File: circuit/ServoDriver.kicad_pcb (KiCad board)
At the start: 2 copper layers, 47 parts, among them IC1 TLP521, IC2 TLP521, IC3 TLP521, IC4 TLP521, IC5 TLP521, IC6 TLP521, J1 RJ45_8pin, J2 RJ45_8pin, J3 servo0, J4 servo1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

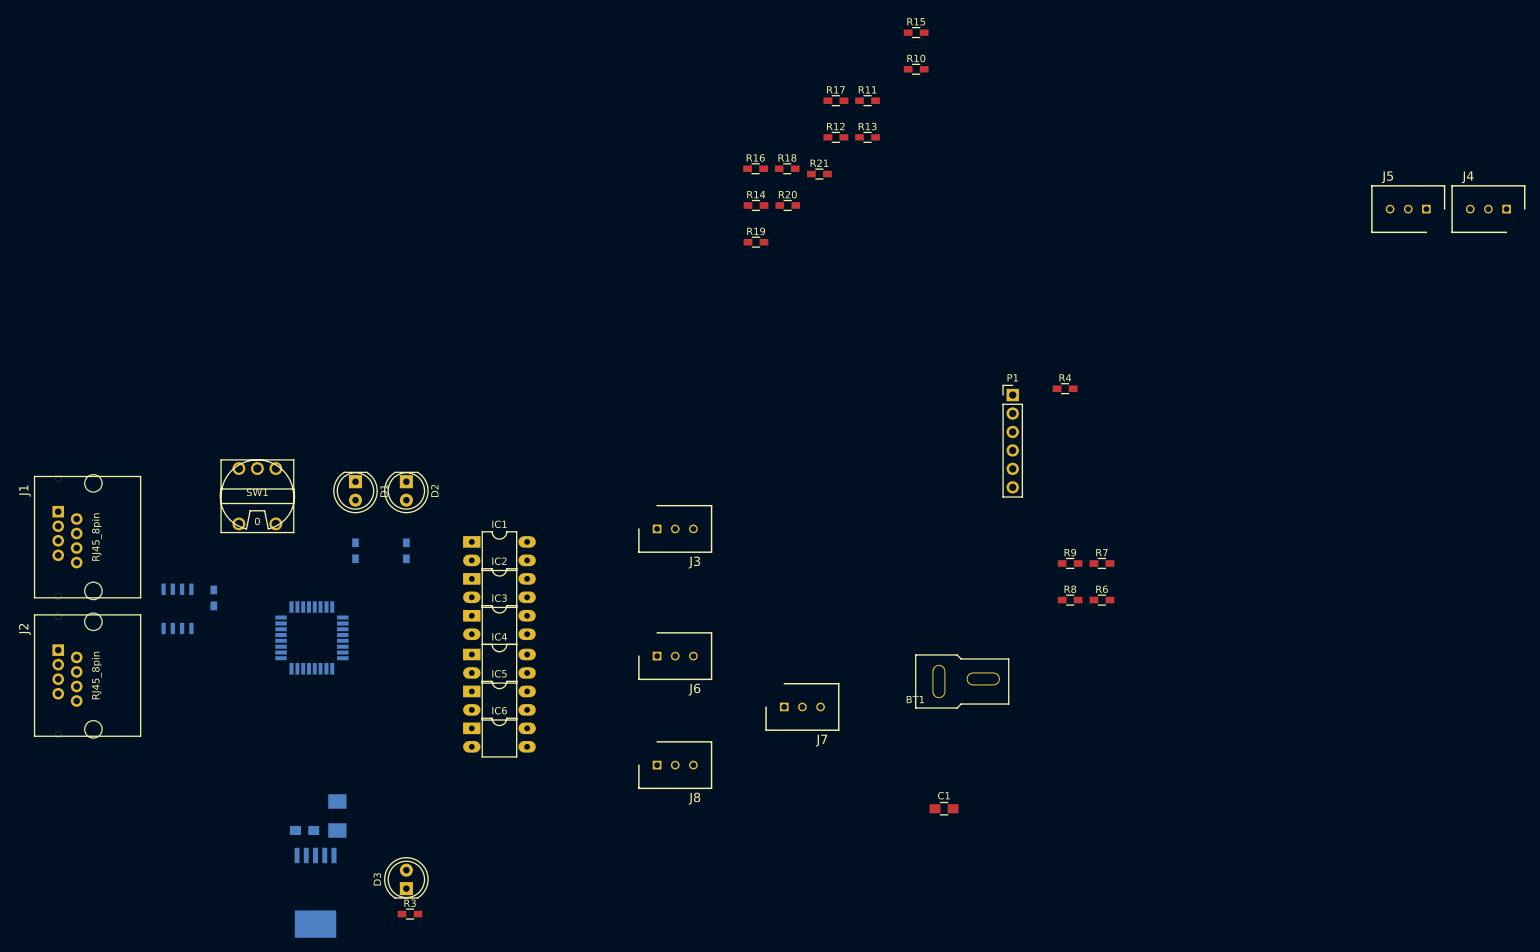
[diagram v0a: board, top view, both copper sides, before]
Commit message: 実態配線図の部品配置を大まかに決定
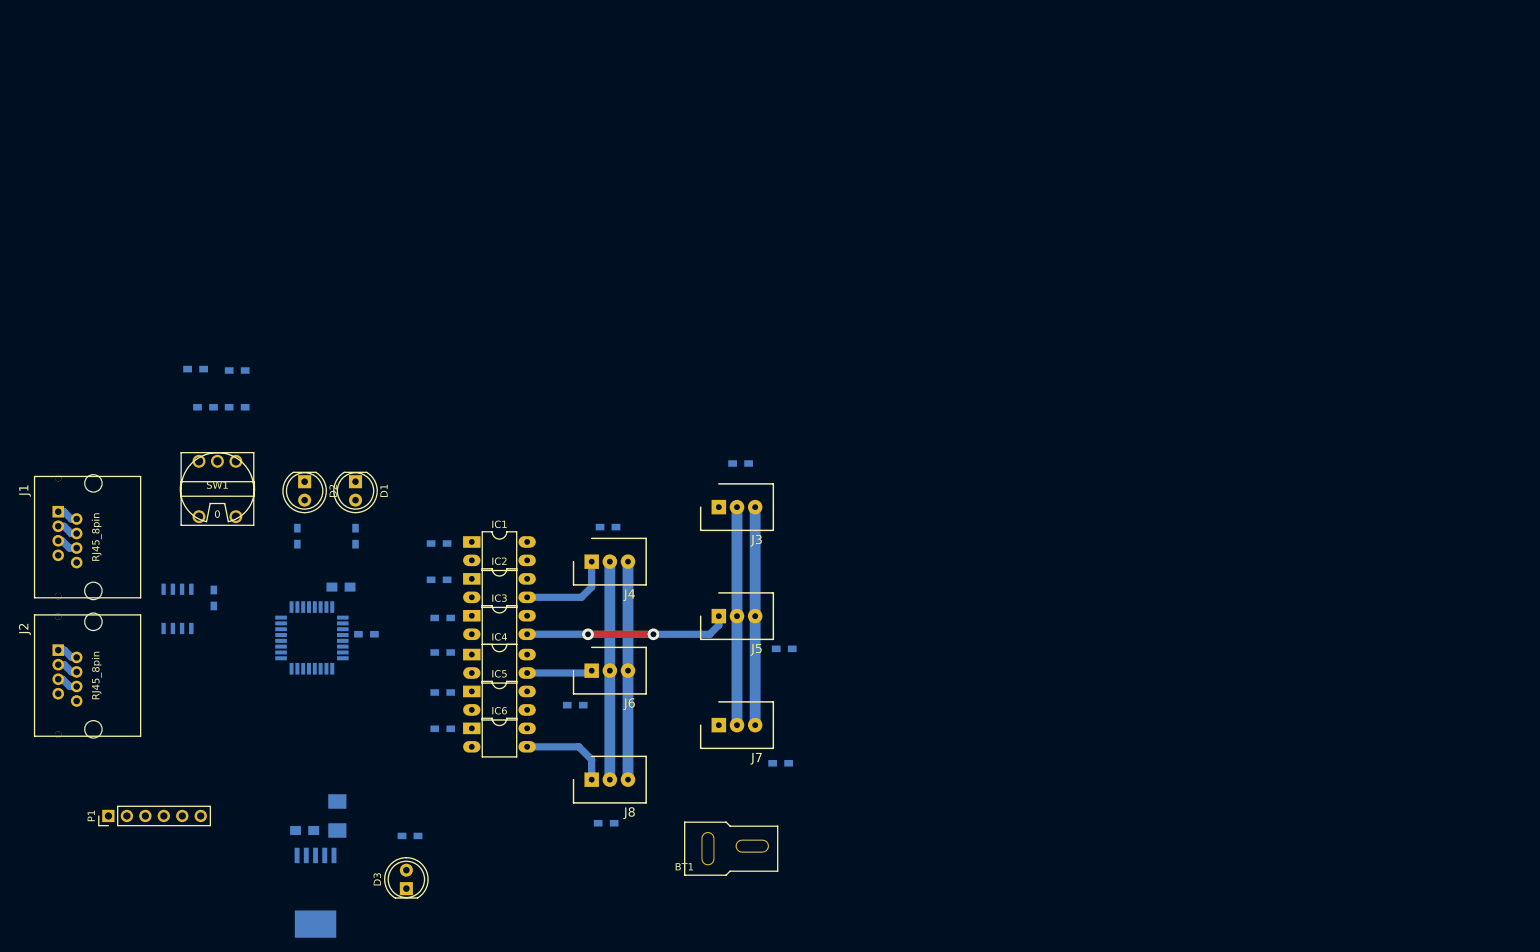
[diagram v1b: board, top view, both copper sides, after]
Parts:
- C1, R10, R11, R12, R13, R14, R15, R16, R17, R18, R19, R20, R21, R3, R4, R6, R7, R8, R9: moved to B.Cu
- J3, J4, J5, J6, J7, J8: footprint YASU:XA_3Pin -> YASU:XA_3Pin_LP
- moved P1 137.3 mm to (92.0, 126.0), turned to 90 degrees
- moved J4 134.9 mm to (158.5, 91.0), turned to 180 degrees
- moved R8 124.5 mm to (104.0, 64.5)
- moved R6 123.1 mm to (109.7, 64.7)
- moved R7 120.9 mm to (109.7, 69.8)
- moved R9 120.9 mm to (105.4, 69.8)
- moved J5 112.3 mm to (176.0, 98.5), turned to 180 degrees
- moved R4 101.9 mm to (127.5, 101.0), turned to 180 degrees
- moved R17 97.8 mm to (138.0, 109.0), turned to 180 degrees
- moved R21 94.0 mm to (160.5, 127.0)
- moved R10 92.6 mm to (137.5, 88.5), turned to 180 degrees
- moved R18 90.5 mm to (138.0, 114.0), turned to 180 degrees
- moved R11 88.5 mm to (137.5, 93.5), turned to 180 degrees
- moved C1 88.4 mm to (124.0, 94.5), turned to 180 degrees
- moved R15 86.7 mm to (185.0, 103.0)
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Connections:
- IC1 pad 1: /Servo0 -> Net-(IC1-Pad1)
- IC1 pad 2: Net-(IC1-Pad2) -> GND
- IC2 pad 1: /Servo1 -> Net-(IC2-Pad1)
- IC2 pad 2: Net-(IC2-Pad2) -> GND
- IC3 pad 1: /Servo2 -> Net-(IC3-Pad1)
- IC3 pad 2: Net-(IC3-Pad2) -> GND
- IC4 pad 1: /Servo3 -> Net-(IC4-Pad1)
- IC4 pad 2: Net-(IC4-Pad2) -> GND
- IC5 pad 1: /Servo4 -> Net-(IC5-Pad1)
- IC5 pad 2: Net-(IC5-Pad2) -> GND
- IC6 pad 1: /Servo5 -> Net-(IC6-Pad1)
- IC6 pad 2: Net-(IC6-Pad2) -> GND
- R10 pad 1: Net-(IC1-Pad2) -> Net-(IC1-Pad1)
- R10 pad 2: GND -> /Servo0
- R11 pad 1: Net-(IC2-Pad2) -> Net-(IC2-Pad1)
- R11 pad 2: GND -> /Servo1
- R12 pad 1: Net-(IC3-Pad2) -> Net-(IC3-Pad1)
- R12 pad 2: GND -> /Servo2
- R16 pad 1: Net-(IC4-Pad2) -> Net-(IC4-Pad1)
- R16 pad 2: GND -> /Servo3
- R17 pad 1: Net-(IC5-Pad2) -> Net-(IC5-Pad1)
- R17 pad 2: GND -> /Servo4
- R18 pad 1: Net-(IC6-Pad2) -> Net-(IC6-Pad1)
- R18 pad 2: GND -> /Servo5
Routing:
- net GNDPWR: track 0.00 -> 60.0 mm
- net +7.4V: track 0.00 -> 60.0 mm
- net Net-(IC3-Pad3): track 0.00 -> 28.1 mm, vias 0 -> 2
- net Net-(IC2-Pad3): track 0.00 -> 13.0 mm
- net Net-(IC6-Pad3): track 0.00 -> 12.4 mm
- net Net-(IC4-Pad3): track 0.00 -> 9.01 mm
- net GND: track 0.00 -> 6.20 mm
- net +5V: track 0.00 -> 5.91 mm
- net +12V: track 0.00 -> 5.91 mm

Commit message: モータ側の配線完了
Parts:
- R13, R14, R15, R19, R20, R21: footprint Resistors_SMD:R_0603_HandSoldering -> Resistors_THT:R_Axial_DIN0207_L6.3mm_D2.5mm_P7.62mm_Horizontal; moved to F.Cu
- moved R13 12.3 mm to (173.5, 88.5)
- moved R15 11.5 mm to (173.5, 103.5)
- moved R20 11.0 mm to (173.5, 118.5)
- moved R14 11.0 mm to (155.8, 96.0)
- moved R21 4.61 mm to (156.0, 126.0)
- moved BT1 4.01 mm to (170.5, 130.2)
- moved R19 0.56 mm to (155.8, 111.0)
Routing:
- net +7.4V: track 60.0 -> 176.3 mm
- net GNDPWR: track 60.0 -> 107.4 mm
- net Net-(IC1-Pad3): track 0.00 -> 34.3 mm, vias 0 -> 2
- net Net-(IC5-Pad3): track 0.00 -> 32.9 mm, vias 0 -> 2
- net Net-(IC4-Pad3): track 9.01 -> 15.9 mm
- net Net-(IC6-Pad3): track 12.4 -> 19.1 mm
- net Net-(IC3-Pad3): track 28.1 -> 31.2 mm

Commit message: コアを斜めにした
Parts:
- moved C2 12.9 mm to (125.8, 117.0)
- moved C3 12.9 mm to (130.2, 115.0)
- moved U3 12.9 mm to (127.2, 121.0)
- moved D3 10.3 mm to (139.8, 128.2)
- moved R3 10.3 mm to (140.2, 121.0)
- moved U1 6.82 mm to (126.8, 102.5), turned to 225 degrees
- moved C1 6.36 mm to (119.5, 90.0)
- moved R4 5.15 mm to (130.0, 96.5), turned to 315 degrees

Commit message: 基板外形線の追加
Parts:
- moved C1 8.06 mm to (126.5, 94.0)
- moved J1 5.50 mm to (87.6, 93.1)
- moved U2 5.00 mm to (101.5, 102.5)
- moved J2 4.50 mm to (87.6, 111.2)
- moved R10 0.79 mm to (138.2, 88.2)
- moved R11 0.75 mm to (138.2, 93.5)
- moved R12 0.35 mm to (138.2, 98.5)
- moved R16 0.35 mm to (138.2, 103.8)
- moved R18 0.25 mm to (138.2, 114.0)
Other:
- board outline added: 102.5 x 54.5 mm
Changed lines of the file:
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@@
     (area 78.9718 61.975 195.176192 142.956775)
     (thickness 1.6)
-    (drawings 0)
-    (tracks 137)
+    (drawings 4)
+    (tracks 136)
     (zones 0)
     (modules 47)
@@
     (pad_to_mask_clearance 0.2)
     (aux_axis_origin 0 0)
-    (visible_elements 7FFFFFFF)
+    (visible_elements 7FFFF7FF)
     (pcbplotparams
       (layerselection 0x00030_80000001)
@@
     (add_net "Net-(U3-Pad4)")
   )
+  (module Resistors_SMD:R_0603_HandSoldering (layer B.Cu)
+    (at 138.25 88.25 180)
+    (descr "Resistor SMD 0603, hand soldering")
+    (tags "resistor 0603")
+    (attr smd)
+    (fp_text reference R10 (at 0 1.45 180) (layer B.SilkS)
+      (effects (font (size 1 1) (thickness 0.15)) (justify mirror))
+    )
+    (fp_text value 1k (at 0 -1.55 180) (layer B.Fab)
+      (effects (font (size 1 1) (thickness 0.15)) (justify mirror))
+    )
+    (fp_text user %R (at 0 0 180) (layer B.Fab)
+      (effects (font (size 0.4 0.4) (thickness 0.075)) (justify mirror))
+    )
+    (fp_line (start -0.8 -0.4) (end -0.8 0.4) (layer B.Fab) (width 0.1))
+    (fp_line (start 0.8 -0.4) (end -0.8 -0.4) (layer B.Fab) (width 0.1))
+    (fp_line (start 0.8 0.4) (end 0.8 -0.4) (layer B.Fab) (width 0.1))
+    (fp_line (start -0.8 0.4) (end 0.8 0.4) (layer B.Fab) (width 0.1))
+    (fp_line (start 0.5 -0.68) (end -0.5 -0.68) (layer B.SilkS) (width 0.12))
+    (fp_line (start -0.5 0.68) (end 0.5 0.68) (layer B.SilkS) (width 0.12))
+    (fp_line (start -1.96 0.7) (end 1.95 0.7) (layer B.CrtYd) (width 0.05))
+    (fp_line (start -1.96 0.7) (end -1.96 -0.7) (layer B.CrtYd) (width 0.05))
+    (fp_line (start 1.95 -0.7) (end 1.95 0.7) (layer B.CrtYd) (width 0.05))
+    (fp_line (start 1.95 -0.7) (end -1.96 -0.7) (layer B.CrtYd) (width 0.05))
+    (pad 1 smd rect (at -1.1 0 180) (size 1.2 0.9) (layers B.Cu B.Paste B.Mask)
+      (net 49 "Net-(IC1-Pad1)"))
+    (pad 2 smd rect (at 1.1 0 180) (size 1.2 0.9) (layers B.Cu B.Paste B.Mask)
+      (net 9 /Servo0))
+    (model ${KISYS3DMOD}/Resistors_SMD.3dshapes/R_0603.wrl
+      (at (xyz 0 0 0))
+      (scale (xyz 1 1 1))
+      (rotate (xyz 0 0 0))
+    )
+  )
   (module YASU:XA_3Pin_LP (layer F.Cu)
     (at 176 98.5 180)
@@
   )
   (module Capacitors_SMD:C_0805_HandSoldering (layer B.Cu)
-    (at 119.5 90 180)
+    (at 126.5 94 180)
     (descr "Capacitor SMD 0805, hand soldering")
     (tags "capacitor 0805")
@@
   )
   (module robocon_pcb:7810-8P8C (layer F.Cu)
-    (at 87.63 87.63 90)
+    (at 87.63 93.13 90)
     (tags RJ45)
     (fp_text reference J1 (at 6.477 -7.239 90) (layer F.SilkS)
@@
   )
   (module robocon_pcb:7810-8P8C (layer F.Cu)
-    (at 87.63 106.68 90)
+    (at 87.63 111.18 90)
     (tags RJ45)
     (fp_text reference J2 (at 6.477 -7.239 90) (layer F.SilkS)
@@
   )
   (module Resistors_SMD:R_0603_HandSoldering (layer B.Cu)
-    (at 137.5 88.5 180)
-    (descr "Resistor SMD 0603, hand soldering")
-    (tags "resistor 0603")
-    (attr smd)
-    (fp_text reference R10 (at 0 1.45 180) (layer B.SilkS)
-      (effects (font (size 1 1) (thickness 0.15)) (justify mirror))
-    )
-    (fp_text value 1k (at 0 -1.55 180) (layer B.Fab)
-      (effects (font (size 1 1) (thickness 0.15)) (justify mirror))
-    )
-    (fp_text user %R (at 0 0 180) (layer B.Fab)
-      (effects (font (size 0.4 0.4) (thickness 0.075)) (justify mirror))
-    )
-    (fp_line (start -0.8 -0.4) (end -0.8 0.4) (layer B.Fab) (width 0.1))
-    (fp_line (start 0.8 -0.4) (end -0.8 -0.4) (layer B.Fab) (width 0.1))
-    (fp_line (start 0.8 0.4) (end 0.8 -0.4) (layer B.Fab) (width 0.1))
-    (fp_line (start -0.8 0.4) (end 0.8 0.4) (layer B.Fab) (width 0.1))
-    (fp_line (start 0.5 -0.68) (end -0.5 -0.68) (layer B.SilkS) (width 0.12))
-    (fp_line (start -0.5 0.68) (end 0.5 0.68) (layer B.SilkS) (width 0.12))
-    (fp_line (start -1.96 0.7) (end 1.95 0.7) (layer B.CrtYd) (width 0.05))
-    (fp_line (start -1.96 0.7) (end -1.96 -0.7) (layer B.CrtYd) (width 0.05))
-    (fp_line (start 1.95 -0.7) (end 1.95 0.7) (layer B.CrtYd) (width 0.05))
-    (fp_line (start 1.95 -0.7) (end -1.96 -0.7) (layer B.CrtYd) (width 0.05))
-    (pad 1 smd rect (at -1.1 0 180) (size 1.2 0.9) (layers B.Cu B.Paste B.Mask)
-      (net 49 "Net-(IC1-Pad1)"))
-    (pad 2 smd rect (at 1.1 0 180) (size 1.2 0.9) (layers B.Cu B.Paste B.Mask)
-      (net 9 /Servo0))
-    (model ${KISYS3DMOD}/Resistors_SMD.3dshapes/R_0603.wrl
-      (at (xyz 0 0 0))
-      (scale (xyz 1 1 1))
-      (rotate (xyz 0 0 0))
-    )
-  )
-  (module Resistors_SMD:R_0603_HandSoldering (layer B.Cu)
-    (at 137.5 93.5 180)
+    (at 138.25 93.5 180)
     (descr "Resistor SMD 0603, hand soldering")
     (tags "resistor 0603")
@@
   )
   (module Resistors_SMD:R_0603_HandSoldering (layer B.Cu)
-    (at 138 98.75 180)
+    (at 138.25 98.5 180)
     (descr "Resistor SMD 0603, hand soldering")
     (tags "resistor 0603")
@@
   )
   (module Resistors_SMD:R_0603_HandSoldering (layer B.Cu)
-    (at 138 103.5 180)
+    (at 138.25 103.75 180)
     (descr "Resistor SMD 0603, hand soldering")
     (tags "resistor 0603")
@@
   )
   (module Resistors_SMD:R_0603_HandSoldering (layer B.Cu)
-    (at 138 114 180)
+    (at 138.25 114 180)
     (descr "Resistor SMD 0603, hand soldering")
     (tags "resistor 0603")
@@
   )
   (module Housings_SOIC:SOIC-8_3.9x4.9mm_Pitch1.27mm (layer B.Cu)
-    (at 101.5 97.5 90)
+    (at 101.5 102.5 90)
     (descr "8-Lead Plastic Small Outline (SN) - Narrow, 3.90 mm Body [SOIC] (see Microchip Packaging Specification 00000049BS.pdf)")
     (tags "SOIC 1.27")
@@
     )
   )
+  (gr_line (start 81.5 134.25) (end 184 134.25) (angle 90) (layer Edge.Cuts) (width 0.15))
+  (gr_line (start 81.5 79.75) (end 81.5 134.25) (angle 90) (layer Edge.Cuts) (width 0.15))
+  (gr_line (start 184 79.75) (end 81.5 79.75) (angle 90) (layer Edge.Cuts) (width 0.15))
+  (gr_line (start 184 134.25) (end 184 79.75) (angle 90) (layer Edge.Cuts) (width 0.15))
   (segment (start 161 88.75) (end 161 83.5) (width 1.5) (layer B.Cu) (net 1))
   (segment (start 163.75 80.75) (end 175.75 80.75) (width 1.5) (layer B.Cu) (net 1))
@@
   (segment (start 163.5 106) (end 163.5 97.75) (width 1.5) (layer B.Cu) (net 2))
   (segment (start 163.5 97.75) (end 163.5 91) (width 1.5) (layer B.Cu) (net 2))
-  (segment (start 85.09 107.18) (end 85.68 107.18) (width 1) (layer B.Cu) (net 4))
-  (segment (start 85.68 107.18) (end 86.68 108.18) (width 1) (layer B.Cu) (net 4))
-  (segment (start 86.68 108.18) (end 87.63 108.18) (width 1) (layer B.Cu) (net 4))
-  (segment (start 85.09 88.13) (end 85.63 88.13) (width 1) (layer B.Cu) (net 4))
-  (segment (start 85.63 88.13) (end 86.63 89.13) (width 1) (layer B.Cu) (net 4))
-  (segment (start 86.63 89.13) (end 87.63 89.13) (width 1) (layer B.Cu) (net 4))
-  (segment (start 85.09 88.13) (end 85.38 88.13) (width 1) (layer B.Cu) (net 4))
-  (segment (start 85.09 105.18) (end 85.93 105.18) (width 1) (layer B.Cu) (net 5))
-  (segment (start 85.93 105.18) (end 86.93 106.18) (width 1) (layer B.Cu) (net 5))
-  (segment (start 86.93 106.18) (end 87.63 106.18) (width 1) (layer B.Cu) (net 5))
-  (segment (start 87.63 87.13) (end 86.88 87.13) (width 1) (layer B.Cu) (net 5))
-  (segment (start 86.88 87.13) (end 85.88 86.13) (width 1) (layer B.Cu) (net 5))
-  (segment (start 85.88 86.13) (end 85.09 86.13) (width 1) (layer B.Cu) (net 5))
-  (segment (start 136 88.5) (end 136.4 88.5) (width 0.5) (layer B.Cu) (net 9))
+  (segment (start 85.09 111.68) (end 85.68 111.68) (width 1) (layer B.Cu) (net 4))
+  (segment (start 85.68 111.68) (end 86.68 112.68) (width 1) (layer B.Cu) (net 4))
+  (segment (start 86.68 112.68) (end 87.63 112.68) (width 1) (layer B.Cu) (net 4))
+  (segment (start 85.09 93.63) (end 85.63 93.63) (width 1) (layer B.Cu) (net 4))
+  (segment (start 85.63 93.63) (end 86.63 94.63) (width 1) (layer B.Cu) (net 4))
+  (segment (start 86.63 94.63) (end 87.63 94.63) (width 1) (layer B.Cu) (net 4))
+  (segment (start 85.09 93.63) (end 85.38 93.63) (width 1) (layer B.Cu) (net 4))
+  (segment (start 85.09 109.68) (end 85.93 109.68) (width 1) (layer B.Cu) (net 5))
+  (segment (start 85.93 109.68) (end 86.93 110.68) (width 1) (layer B.Cu) (net 5))
+  (segment (start 86.93 110.68) (end 87.63 110.68) (width 1) (layer B.Cu) (net 5))
+  (segment (start 87.63 92.63) (end 86.88 92.63) (width 1) (layer B.Cu) (net 5))
+  (segment (start 86.88 92.63) (end 85.88 91.63) (width 1) (layer B.Cu) (net 5))
+  (segment (start 85.88 91.63) (end 85.09 91.63) (width 1) (layer B.Cu) (net 5))
   (segment (start 176 83.5) (end 176 84.25) (width 1) (layer B.Cu) (net 10))
   (segment (start 176 84.25) (end 174.5 85.75) (width 1) (layer B.Cu) (net 10))
@@
   (segment (start 158.5 118.25) (end 158.5 121) (width 1) (layer B.Cu) (net 20))
   (segment (start 156.734 116.484) (end 158.5 118.25) (width 1) (layer B.Cu) (net 20))
-  (segment (start 85.09 103.18) (end 85.93 103.18) (width 1) (layer B.Cu) (net 22))
-  (segment (start 85.93 103.18) (end 86.93 104.18) (width 1) (layer B.Cu) (net 22))
-  (segment (start 86.93 104.18) (end 87.63 104.18) (width 1) (layer B.Cu) (net 22))
-  (segment (start 85.09 84.13) (end 85.88 84.13) (width 1) (layer B.Cu) (net 22))
-  (segment (start 85.88 84.13) (end 86.88 85.13) (width 1) (layer B.Cu) (net 22))
-  (segment (start 86.88 85.13) (end 87.63 85.13) (width 1) (layer B.Cu) (net 22))
+  (segment (start 85.09 107.68) (end 85.93 107.68) (width 1) (layer B.Cu) (net 22))
+  (segment (start 85.93 107.68) (end 86.93 108.68) (width 1) (layer B.Cu) (net 22))
+  (segment (start 86.93 108.68) (end 87.63 108.68) (width 1) (layer B.Cu) (net 22))
+  (segment (start 85.09 89.63) (end 85.88 89.63) (width 1) (layer B.Cu) (net 22))
+  (segment (start 85.88 89.63) (end 86.88 90.63) (width 1) (layer B.Cu) (net 22))
+  (segment (start 86.88 90.63) (end 87.63 90.63) (width 1) (layer B.Cu) (net 22))
 )
